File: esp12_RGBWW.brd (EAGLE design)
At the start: 47 x 53 mm, 30 parts

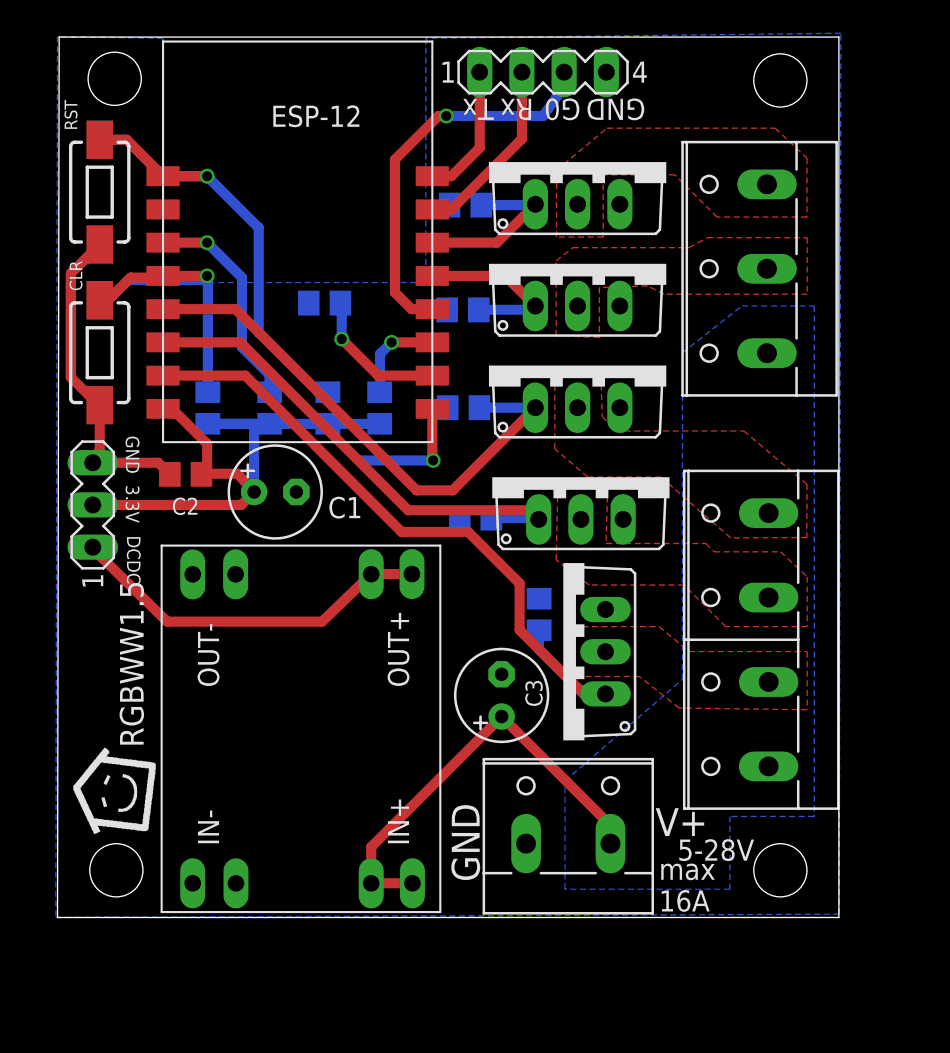
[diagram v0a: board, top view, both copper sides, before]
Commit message: new, smaller board
new design, integrated DCDC converter, new, smaller MOSFETs, smaller overal board, additional PRG button, mostly optimized for SMD manufacturing but still hand solderable
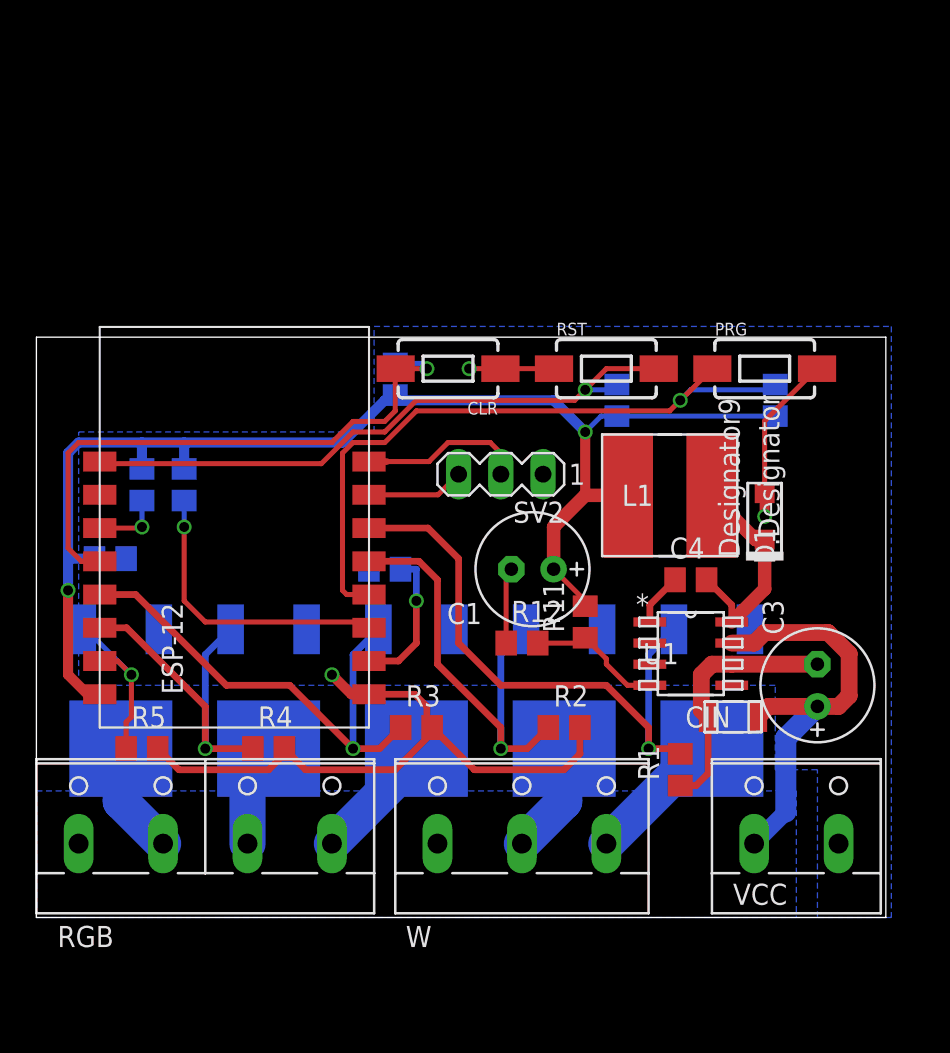
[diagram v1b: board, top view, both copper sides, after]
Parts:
- removed CLR1, RST1: (no value), SparkFun-Electromechanical:TACTILE-SWITCH-1101NE
- removed IRLZ44N-B, IRLZ44N-CW, IRLZ44N-G, IRLZ44N-R, IRLZ44N-WW: (no value), PAsystem:TO220AV
- removed PROG: (no value), con-lstb:MA04-1
- removed SV1: (no value), con-lstb:MA03-1
- removed U$1: (no value), fhem.logo:LOGO
- removed U$2: XM1584, XM1584:XM1584-TH
- added C4: 10nF, resistor:C0805
- added CIN: 4.7uF, AcceleratedDesigns_Lib:1206
- added D1: 570mV, AcceleratedDesigns_Lib:SOD-123F
- added L1: 56uH, AcceleratedDesigns_Lib:IND_NPI75C
- added PRG: (no value), SparkFun-Electromechanical:TACTILE-SWITCH-1101NE
- added Q1, Q2, Q3, Q4, Q5: AOD2910SMD, transistor-fet+irf7201:DPAK-3
- added R11: 10k, resistor:R0805
- added R12: 5.9k, resistor:R0805
- added R13: 10k, rcl:R0805
- added SV2: (no value), con-lstb:MA03-1
- added U1: TPS5410DR, AcceleratedDesigns_Lib:M08A
- C1: device resistor:E2,5-6 -> resistor:E2,5-7
- C3: value (none) -> 240uF; device resistor:E2,5-6 -> resistor:E2,5-7
- moved W 36.8 mm to (27.9, 5.08), turned to 0 degrees
- moved R1 36.3 mm to (37.5, 8.89), flipped to the top, turned to 90 degrees
- moved RGB 35.2 mm to (8.89, 5.08), turned to 0 degrees
- moved RST 32.3 mm to (33.0, 33.0), turned to 0 degrees
- moved R2 25.9 mm to (30.5, 11.4), flipped to the top
- moved R5 25.2 mm to (5.08, 10.2), flipped to the top, turned to 0 degrees
- moved CLR 21.0 mm to (23.5, 33.0), turned to 180 degrees
- moved R3 19.4 mm to (21.6, 11.4), flipped to the top
- moved C3 19.0 mm to (45.7, 14.0)
- moved R4 18.6 mm to (12.7, 10.2), flipped to the top
- moved ESP-12 17.6 mm to (2.54, 11.4)
- moved R10 17.4 mm to (33.7, 31.1)
- moved R6 16.4 mm to (19.7, 21.0)
- moved C1 16.2 mm to (28.6, 21.0), turned to 180 degrees
- moved VCC 13.7 mm to (44.5, 5.08)
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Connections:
- net N$2 renamed CH_PD
- net N$3 renamed G2
- net N$7 renamed G15
- removed net DCDC+: SV1.1, U$2.OUT+(1), U$2.OUT+(2)
- removed net N$1: CLR.2, CLR1.2, ESP-12.12, R8.2
- removed net N$12: ESP-12.9, R10.2, RST.2, RST1.2
- removed net N$9: ESP-12.4, PROG.3
- removed net RGB-B-OUT: IRLZ44N-B.C, RGB.4
- removed net RGB-CW-OUT: IRLZ44N-CW.C, W.2
- removed net RGB-G-OUT: IRLZ44N-G.C, RGB.3
- removed net RGB-R-OUT: IRLZ44N-R.C, RGB.2
- removed net RGB-WW-OUT: IRLZ44N-WW.C, W.3
- new net B: Q5.4, RGB.4
- new net BOOT: C4.1, U1.1
- new net CLR_S: CLR.2, ESP-12.12, R8.2
- new net CW: Q2.4, W.2
- new net G: Q4.4, RGB.3
- new net PH: C4.2, D1.1, L1.2, U1.8
- new net PRG_S: ESP-12.4, PRG.1, R13.1
- new net R: Q3.4, RGB.2
- new net RST_S: ESP-12.9, R10.2, RST.2
- new net SENS: R11.1, R12.2, U1.4
- new net WW: Q1.4, W.3
- net +12V: now also CIN.2, U1.7, VCC.1; no longer U$2.IN+(1), U$2.IN+(2), VCC.2
- net +3V3: now also L1.1, R11.2, R13.2; no longer SV1.2
- net GND: now also CIN.1, D1.2, PRG.2, Q1.3, Q2.3, Q3.3, Q4.3, Q5.3, R12.1, SV2.1, U1.6, VCC.2; no longer CLR1.1, IRLZ44N-B.E, IRLZ44N-CW.E, IRLZ44N-G.E, IRLZ44N-R.E, IRLZ44N-WW.E, PROG.4, RST1.1, SV1.3, U$2.IN-(1), U$2.IN-(2), U$2.OUT-(1), U$2.OUT-(2), VCC.1
- net N$5: now also SV2.3; no longer PROG.2
- net N$8: now also SV2.2; no longer PROG.1
- net RGB-B: now also Q5.1; no longer IRLZ44N-B.B
- net RGB-CW: now also Q2.1; no longer IRLZ44N-CW.B
- net RGB-G: now also Q4.1; no longer IRLZ44N-G.B
- net RGB-R: now also Q3.1; no longer IRLZ44N-R.B
- net RGB-WW: now also Q1.1; no longer IRLZ44N-WW.B
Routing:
- net GND: track 27.2 -> 76.0 mm, vias 1 -> 3
- net +3V3: track 36.2 -> 83.9 mm, vias 0 -> 2
- net PRG_S: track 0.00 -> 40.4 mm, vias 0 -> 1
- net RST_S: track 0.00 -> 38.1 mm, vias 0 -> 1
- net CLR_S: track 0.00 -> 35.4 mm, vias 0 -> 1
- net N$12: track 31.1 -> 0.00 mm, vias 1 -> 0
- net RGB-R: track 42.5 -> 12.0 mm, vias 0 -> 1
- net RGB-WW: track 10.4 -> 35.9 mm, vias 0 -> 1
- net N$9: track 23.7 -> 0.00 mm, vias 1 -> 0
- net DCDC+: track 22.2 -> 0.00 mm
- net N$1: track 21.2 -> 0.00 mm, vias 1 -> 0
- net RGB-CW: track 10.5 -> 27.5 mm, vias 0 -> 1
- net PH: track 0.00 -> 15.7 mm
- net G2: track 5.75 -> 17.8 mm
- net CH_PD: track 13.2 -> 4.16 mm
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- removed copper zone on layer 1, net RGB-B-OUT
- removed copper zone on layer 1, net RGB-CW-OUT
- removed copper zone on layer 1, net RGB-G-OUT
- removed copper zone on layer 1, net RGB-R-OUT
- removed copper zone on layer 1, net RGB-WW-OUT
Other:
- board size 47 x 53 mm -> 51.1 x 34.9 mm
- board text removed: "3.3V"
- board text removed: "5-28V"
- board text removed: "B"
- board text removed: "CW"
- board text removed: "DCDC"
- board text removed: "G"
- board text removed: "G0"
- board text removed: "GND"
- board text removed: "R"
- board text removed: "RGBWW1.5"
- board text removed: "Rx"
- board text removed: "Tx"
- board text removed: "V+"
- board text removed: "WW"
- board text removed: "max 16A"

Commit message: minor placement changes
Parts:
- moved C1 6.35 mm to (28.6, 27.3), turned to 270 degrees
- moved R12 5.24 mm to (26.7, 21.6)
- moved R11 4.02 mm to (30.5, 21.6), turned to 0 degrees
- moved SV2 3.81 mm to (22.9, 26.7), turned to 90 degrees
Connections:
- removed net N$5: ESP-12.7, SV2.3
- removed net N$8: ESP-12.8, SV2.2
- new net RXD: ESP-12.7, SV2.2
- new net TXD: ESP-12.8, SV2.3
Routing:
- net N$8: track 9.94 -> 0.00 mm
- net N$5: track 5.90 -> 0.00 mm
- net SENS: track 8.70 -> 13.8 mm
- net TXD: track 0.00 -> 4.86 mm
- net RXD: track 0.00 -> 4.63 mm
- net RGB-WW: track 35.9 -> 32.4 mm
- net RGB-CW: track 27.5 -> 24.4 mm
- net +3V3: track 83.9 -> 86.9 mm
- net GND: track 76.0 -> 78.0 mm

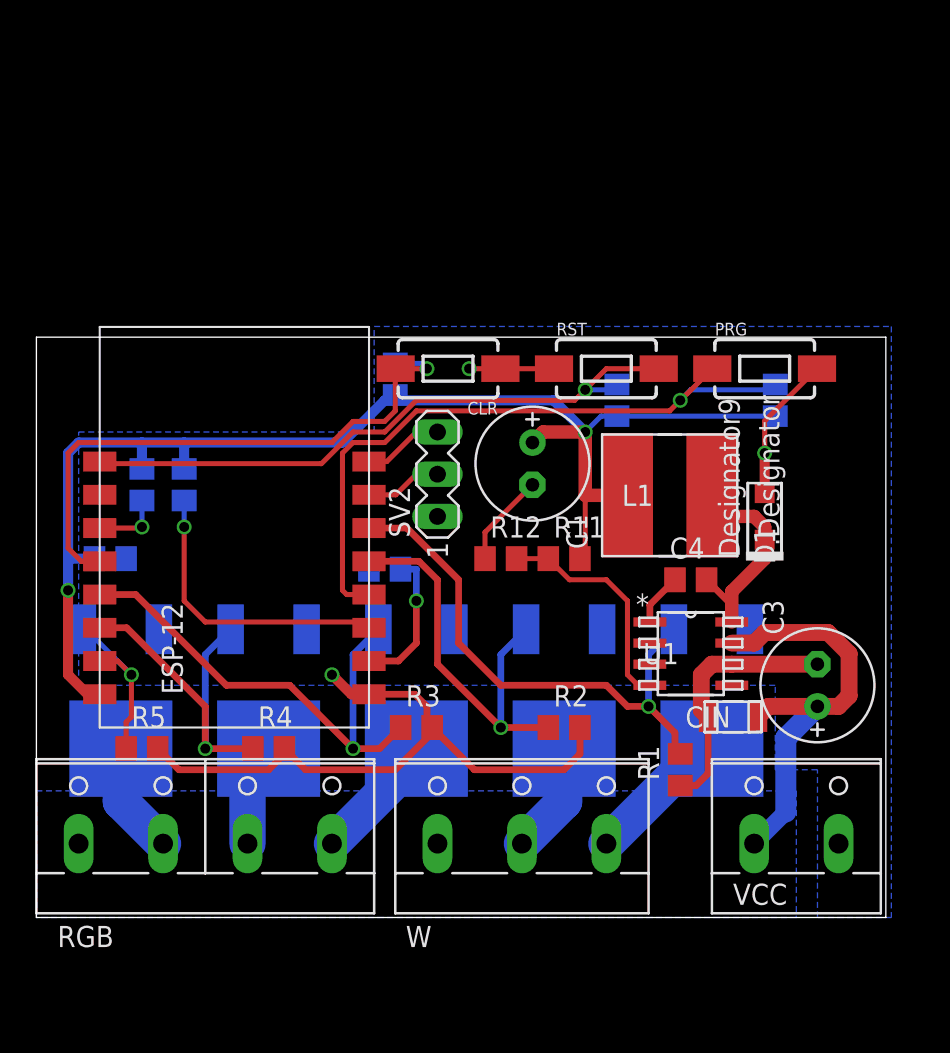
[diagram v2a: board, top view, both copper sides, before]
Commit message: another reduction in size
replaced most of the power supply parts, shaved off another 3mm
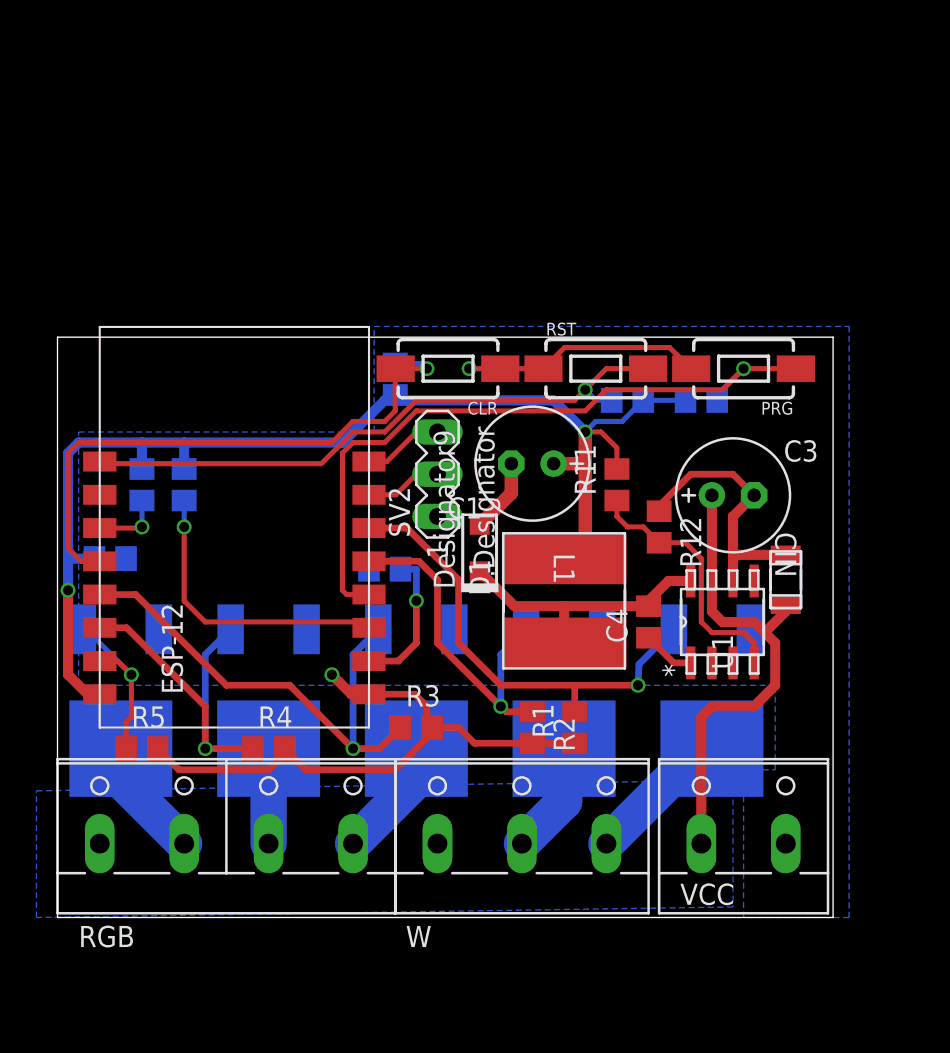
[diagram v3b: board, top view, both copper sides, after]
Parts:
- moved D1 17.3 mm to (25.4, 22.2)
- moved C3 12.5 mm to (40.6, 25.4), turned to 0 degrees
- moved R12 9.71 mm to (36.2, 23.5), turned to 270 degrees
- moved L1 8.98 mm to (30.5, 19.1), turned to 270 degrees
- moved CIN 8.84 mm to (43.8, 20.3), turned to 270 degrees
- moved R1 6.84 mm to (31.1, 11.4)
- moved R11 5.46 mm to (33.7, 26.0), turned to 90 degrees
- moved R13 4.45 mm to (38.7, 31.1), turned to 0 degrees
- moved C4 3.59 mm to (35.6, 17.8), turned to 90 degrees
- moved VCC 3.18 mm to (41.3, 5.08)
- moved U1 2.69 mm to (40.0, 17.8), turned to 90 degrees
- moved R2 1.91 mm to (28.6, 11.4), turned to 270 degrees
- moved PRG 1.27 mm to (41.3, 33.0), turned to 180 degrees
- moved RGB 1.27 mm to (10.2, 5.08)
- moved RST 0.64 mm to (32.4, 33.0)
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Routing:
- net +3V3: track 86.9 -> 73.6 mm
- net GND: track 78.0 -> 72.2 mm, vias 3 -> 2
- net RGB-WW: track 32.4 -> 28.2 mm
- net RGB-CW: track 24.4 -> 21.1 mm
- net +12V: track 26.2 -> 29.2 mm
- net SENS: track 13.8 -> 15.8 mm
- net PRG_S: track 40.4 -> 41.9 mm
- net RST_S: track 38.1 -> 37.3 mm
- net R: track 6.77 -> 7.29 mm
- net B: track 7.82 -> 7.29 mm
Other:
- board size 51.1 x 34.9 mm -> 46.7 x 34.9 mm

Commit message: updated silk screen
some minor changes, mostly cleaned up silk screen
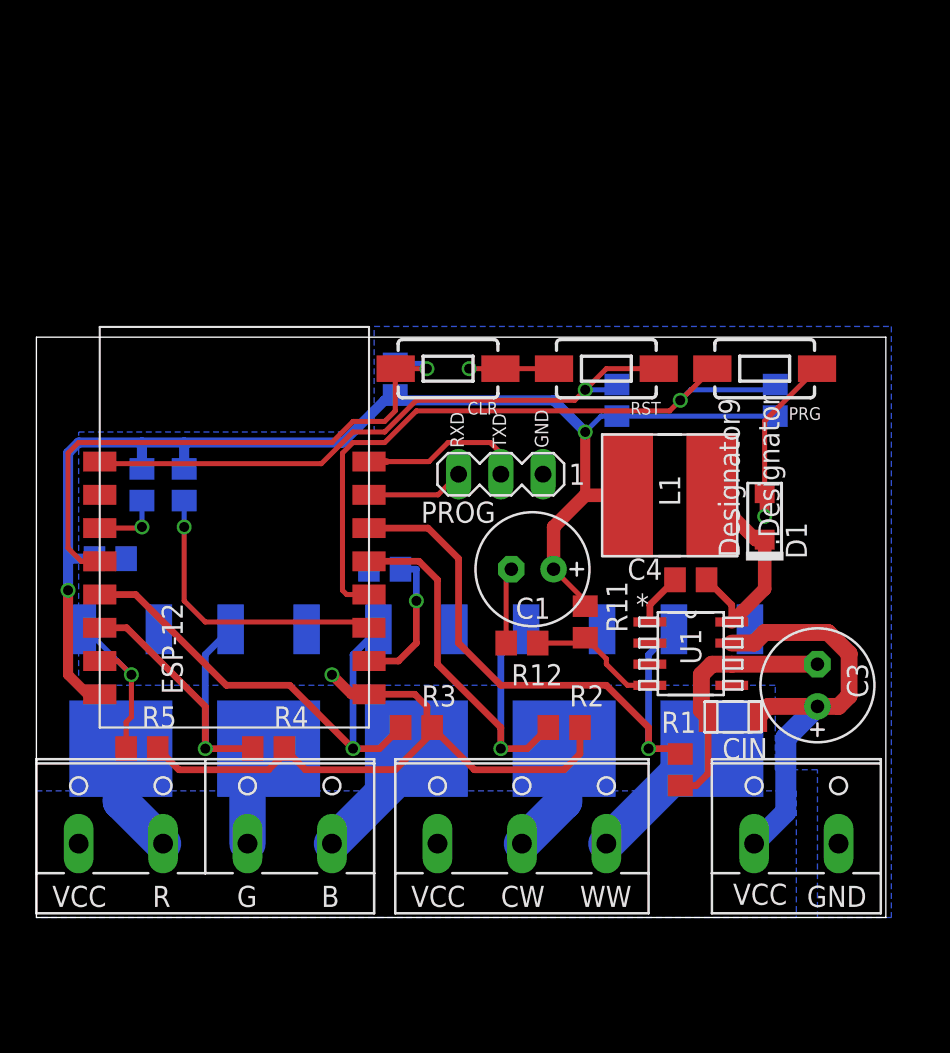
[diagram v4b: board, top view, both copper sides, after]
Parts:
- removed SV2: (no value), con-lstb:MA03-1
- added PROG: (no value), con-lstb:MA03-1
- moved Q3 17.8 mm to (21.6, 10.2)
- moved Q5 17.8 mm to (3.81, 10.2)
- moved D1 17.3 mm to (42.5, 24.1)
- moved C3 12.5 mm to (45.7, 14.0), turned to 90 degrees
- moved R12 10.8 mm to (27.9, 16.5), turned to 0 degrees
- moved L1 8.98 mm to (36.8, 25.4), turned to 0 degrees
- moved CIN 8.84 mm to (40.6, 12.1), turned to 0 degrees
- moved R11 8.47 mm to (31.8, 17.8)
- moved R1 6.84 mm to (37.5, 8.89)
- moved C1 6.35 mm to (28.6, 21.0)
- moved R13 4.45 mm to (43.2, 31.1), turned to 270 degrees
- moved C4 3.59 mm to (38.1, 20.3), turned to 0 degrees
- moved VCC 3.18 mm to (44.5, 5.08)
- moved U1 2.69 mm to (38.1, 15.9), turned to 0 degrees
- moved R2 1.91 mm to (30.5, 11.4), turned to 0 degrees
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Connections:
- net B: now also Q3.4; no longer Q5.4
- net GND: now also PROG.1; no longer SV2.1
- net R: now also Q5.4; no longer Q3.4
- net RGB-B: now also Q3.1; no longer Q5.1
- net RGB-R: now also Q5.1; no longer Q3.1
- net RXD: now also PROG.3; no longer SV2.2
- net TXD: now also PROG.2; no longer SV2.3
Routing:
- net +3V3: track 73.6 -> 83.9 mm
- net RGB-WW: track 28.2 -> 35.9 mm
- net SENS: track 15.8 -> 8.70 mm
- net RGB-CW: track 21.1 -> 27.5 mm
- net TXD: track 4.86 -> 9.94 mm
- net GND: track 72.2 -> 76.0 mm, vias 2 -> 3
- net +12V: track 29.2 -> 26.2 mm
- net PRG_S: track 41.9 -> 40.4 mm
- net RXD: track 4.63 -> 5.90 mm
- net PH: track 16.6 -> 15.7 mm
- net RST_S: track 37.3 -> 38.1 mm
- net R: track 7.29 -> 6.77 mm
- net B: track 7.29 -> 7.82 mm
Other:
- board size 46.7 x 34.9 mm -> 51.1 x 34.9 mm
- board text added: "B"
- board text added: "CW"
- board text added: "G"
- board text added: "GND"
- board text added: "R"
- board text added: "RXD"
- board text added: "TXD"
- board text added: "VCC"
- board text added: "WW"

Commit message: added enable function
I added a pin header to short the TPS5410's ENABLE pin to GND, thus switching off the DC/DC converter, effectively turning the controller completely off.
The controller should function normally, when this is left open. Including a switch that connects those two pins is a way of switching the controller off without disconnecting the 12V supply. Whatever it'll be good for.
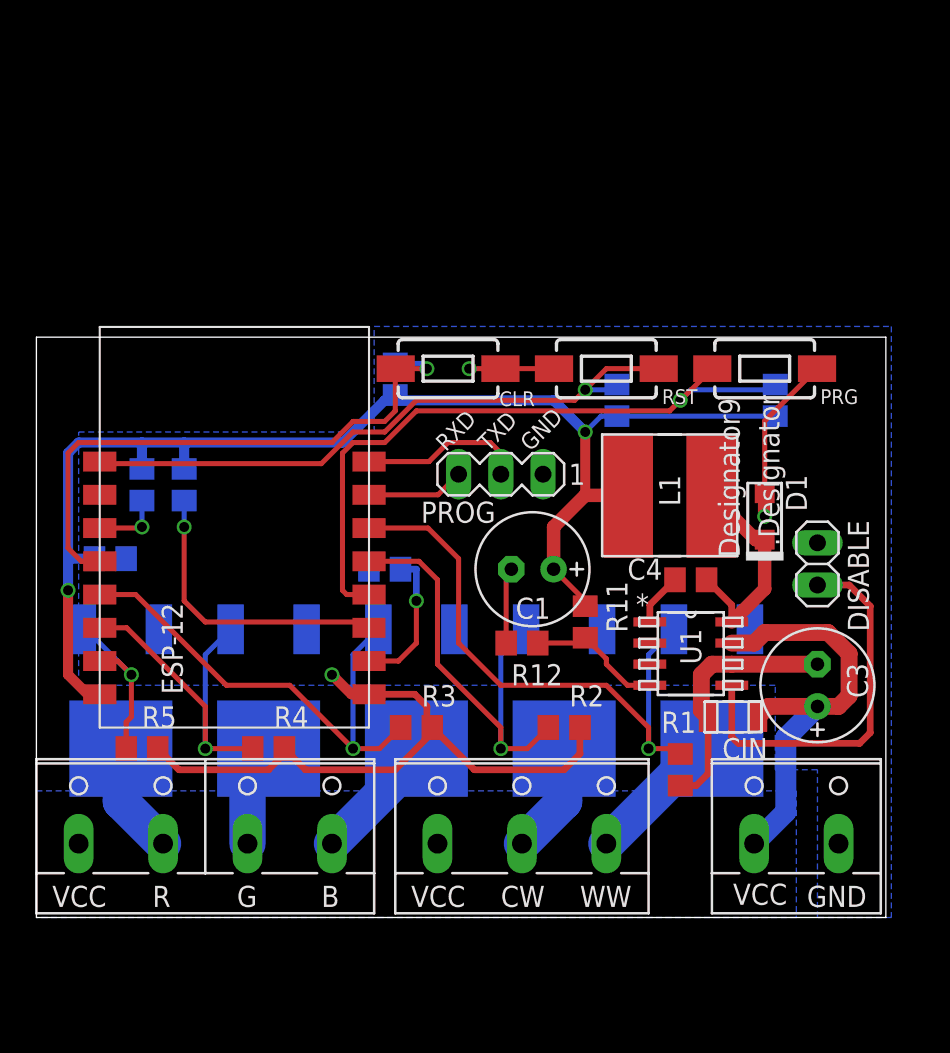
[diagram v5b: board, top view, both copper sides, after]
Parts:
- added DISABLE: (no value), pinhead:1X02
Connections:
- new net ENA: DISABLE.2, U1.5
- net GND: now also DISABLE.1
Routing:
- net ENA: track 0.00 -> 23.2 mm
